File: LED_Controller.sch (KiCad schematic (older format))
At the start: 35 parts, among them CON1 CONNECTOR, CON2 CONNECTOR, CON3 CONNECTOR, CON4 CONNECTOR, CON5 PWR_CON, CON6 AVR-ISP-10, CON7 AVR-ISP-6, IC1 ATMEGA328P-P, Q1 STS8DN3LLH5, Q2 STS8DN3LLH5, Q3 STS8DN3LLH5

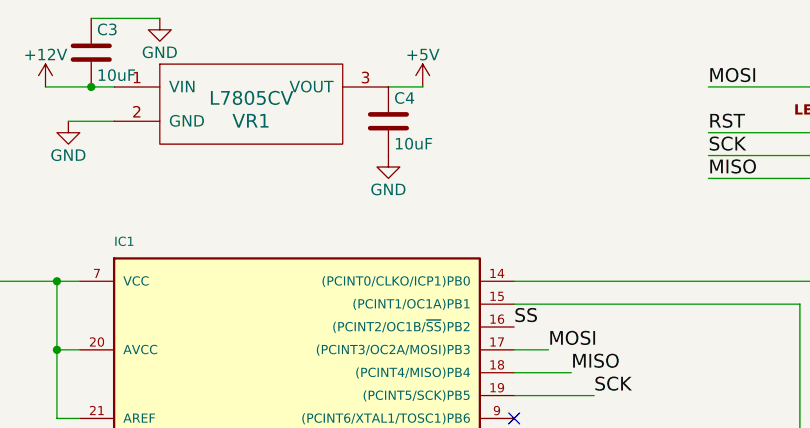
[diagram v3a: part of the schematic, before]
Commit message: Changed passive sizes, re-routed traces
Changed all passive components to 1206 size (that size is stocked in
the lab, and it should be easier to solder without a scope)

Created a general 1206 footprint for resistors and capacitors

Re-routed traces to MOSFETs and rotary encoders, tried to minimize
number of vias
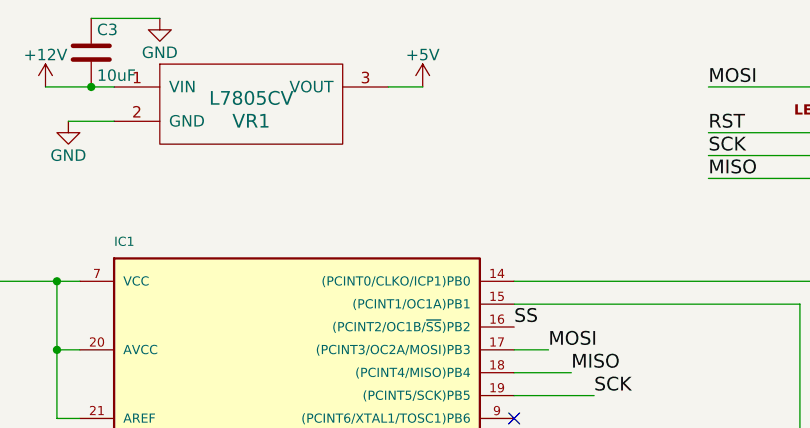
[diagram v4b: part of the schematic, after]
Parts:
- removed C4: 10uF, Capacitors_SMD:C_0603_HandSoldering, symbol C
- C1, C2, R3, R4, R5: footprint Capacitors_SMD:C_0603_HandSoldering -> LED_controller_footprints:SMD_1206
- C3: footprint SMD_Packages:SMD-1206_Pol -> LED_controller_footprints:SMD_1206
- R1, R10, R11, R12, R2, R6, R7: footprint LEDs:LED_0603 -> LED_controller_footprints:SMD_1206
- R8, R9: footprint LEDs:LED_1206 -> LED_controller_footprints:SMD_1206
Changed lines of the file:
@@
 F 0 "R1" V 2130 5350 50  0000 C CNN
 F 1 "10k" V 2050 5350 50  0000 C CNN
-F 2 "LEDs:LED_0603" V 1980 5350 30  0001 C CNN
+F 2 "LED_controller_footprints:SMD_1206" V 1980 5350 30  0001 C CNN
 F 3 "" H 2050 5350 30  0000 C CNN
 	1    2050 5350
@@
 F 0 "R2" V 2130 6250 50  0000 C CNN
 F 1 "10k" V 2050 6250 50  0000 C CNN
-F 2 "LEDs:LED_0603" V 1980 6250 30  0001 C CNN
+F 2 "LED_controller_footprints:SMD_1206" V 1980 6250 30  0001 C CNN
 F 3 "" H 2050 6250 30  0000 C CNN
 	1    2050 6250
@@
 F 0 "R3" V 2130 7250 50  0000 C CNN
 F 1 "10k" V 2050 7250 50  0000 C CNN
-F 2 "Capacitors_SMD:C_0603_HandSoldering" V 1980 7250 30  0001 C CNN
+F 2 "LED_controller_footprints:SMD_1206" V 1980 7250 30  0001 C CNN
 F 3 "" H 2050 7250 30  0000 C CNN
 	1    2050 7250
@@
 F 0 "C1" H 775 2450 50  0000 L CNN
 F 1 "10uF" H 775 2250 50  0000 L CNN
-F 2 "Capacitors_SMD:C_0603_HandSoldering" H 788 2200 30  0001 C CNN
+F 2 "LED_controller_footprints:SMD_1206" H 788 2200 30  0001 C CNN
 F 3 "" H 750 2350 60  0000 C CNN
 	1    750  2350
@@
 F 0 "C2" H 1075 2450 50  0000 L CNN
 F 1 ".1uF" H 1075 2250 50  0000 L CNN
-F 2 "Capacitors_SMD:C_0603_HandSoldering" H 1088 2200 30  0001 C CNN
+F 2 "LED_controller_footprints:SMD_1206" H 1088 2200 30  0001 C CNN
 F 3 "" H 1050 2350 60  0000 C CNN
 	1    1050 2350
@@
 F 0 "R4" V 3830 5000 50  0000 C CNN
 F 1 "10k" V 3750 5000 50  0000 C CNN
-F 2 "Capacitors_SMD:C_0603_HandSoldering" V 3680 5000 30  0001 C CNN
+F 2 "LED_controller_footprints:SMD_1206" V 3680 5000 30  0001 C CNN
 F 3 "" H 3750 5000 30  0000 C CNN
 	1    3750 5000
@@
 F 0 "R5" V 3830 5900 50  0000 C CNN
 F 1 "10k" V 3750 5900 50  0000 C CNN
-F 2 "Capacitors_SMD:C_0603_HandSoldering" V 3680 5900 30  0001 C CNN
+F 2 "LED_controller_footprints:SMD_1206" V 3680 5900 30  0001 C CNN
 F 3 "" H 3750 5900 30  0000 C CNN
 	1    3750 5900
@@
 F 0 "R6" V 3830 6900 50  0000 C CNN
 F 1 "10k" V 3750 6900 50  0000 C CNN
-F 2 "LEDs:LED_0603" V 3680 6900 30  0001 C CNN
+F 2 "LED_controller_footprints:SMD_1206" V 3680 6900 30  0001 C CNN
 F 3 "" H 3750 6900 30  0000 C CNN
 	1    3750 6900
@@
 F 0 "C3" H 2125 950 50  0000 L CNN
 F 1 "10uF" H 2125 750 50  0000 L CNN
-F 2 "SMD_Packages:SMD-1206_Pol" H 2138 700 30  0001 C CNN
+F 2 "LED_controller_footprints:SMD_1206" H 2138 700 30  0001 C CNN
 F 3 "" H 2100 850 60  0000 C CNN
 	1    2100 850
-	1    0    0    -1
-$EndComp
-$Comp
-L C C4
-U 1 1 56B785EB
-P 3400 1150
-F 0 "C4" H 3425 1250 50  0000 L CNN
-F 1 "10uF" H 3425 1050 50  0000 L CNN
-F 2 "Capacitors_SMD:C_0603_HandSoldering" H 3438 1000 30  0001 C CNN
-F 3 "" H 3400 1150 60  0000 C CNN
-	1    3400 1150
-	1    0    0    -1
-$EndComp
-$Comp
-L GND #PWR015
-U 1 1 56B786A8
-P 3400 1300
-F 0 "#PWR015" H 3400 1050 50  0001 C CNN
-F 1 "GND" H 3400 1150 50  0000 C CNN
-F 2 "" H 3400 1300 60  0000 C CNN
-F 3 "" H 3400 1300 60  0000 C CNN
-	1    3400 1300
 	1    0    0    -1
 $EndComp
@@
 F 0 "R7" V 1580 3150 50  0000 C CNN
 F 1 "10k" V 1500 3150 50  0000 C CNN
-F 2 "LEDs:LED_0603" V 1430 3150 30  0001 C CNN
+F 2 "LED_controller_footprints:SMD_1206" V 1430 3150 30  0001 C CNN
 F 3 "" H 1500 3150 30  0000 C CNN
 	1    1500 3150
@@
 F 0 "R8" V 780 5600 50  0000 C CNN
 F 1 "820" V 700 5600 50  0000 C CNN
-F 2 "LEDs:LED_1206" V 630 5600 30  0001 C CNN
+F 2 "LED_controller_footprints:SMD_1206" V 630 5600 30  0001 C CNN
 F 3 "" H 700 5600 30  0000 C CNN
 	1    700  5600
@@
 F 0 "R9" V 1130 5600 50  0000 C CNN
 F 1 "499" V 1050 5600 50  0000 C CNN
-F 2 "LEDs:LED_1206" V 980 5600 30  0001 C CNN
+F 2 "LED_controller_footprints:SMD_1206" V 980 5600 30  0001 C CNN
 F 3 "" H 1050 5600 30  0000 C CNN
 	1    1050 5600
@@
 F 0 "R10" V 5980 2600 50  0000 C CNN
 F 1 "10k" V 5900 2600 50  0000 C CNN
-F 2 "LEDs:LED_0603" V 5830 2600 30  0001 C CNN
+F 2 "LED_controller_footprints:SMD_1206" V 5830 2600 30  0001 C CNN
 F 3 "" H 5900 2600 30  0000 C CNN
 	1    5900 2600
@@
 F 0 "R11" V 5980 3700 50  0000 C CNN
 F 1 "10k" V 5900 3700 50  0000 C CNN
-F 2 "LEDs:LED_0603" V 5830 3700 30  0001 C CNN
+F 2 "LED_controller_footprints:SMD_1206" V 5830 3700 30  0001 C CNN
 F 3 "" H 5900 3700 30  0000 C CNN
 	1    5900 3700
@@
 F 0 "R12" V 5980 4950 50  0000 C CNN
 F 1 "10k" V 5900 4950 50  0000 C CNN
-F 2 "LEDs:LED_0603" V 5830 4950 30  0001 C CNN
+F 2 "LED_controller_footprints:SMD_1206" V 5830 4950 30  0001 C CNN
 F 3 "" H 5900 4950 30  0000 C CNN
 	1    5900 4950

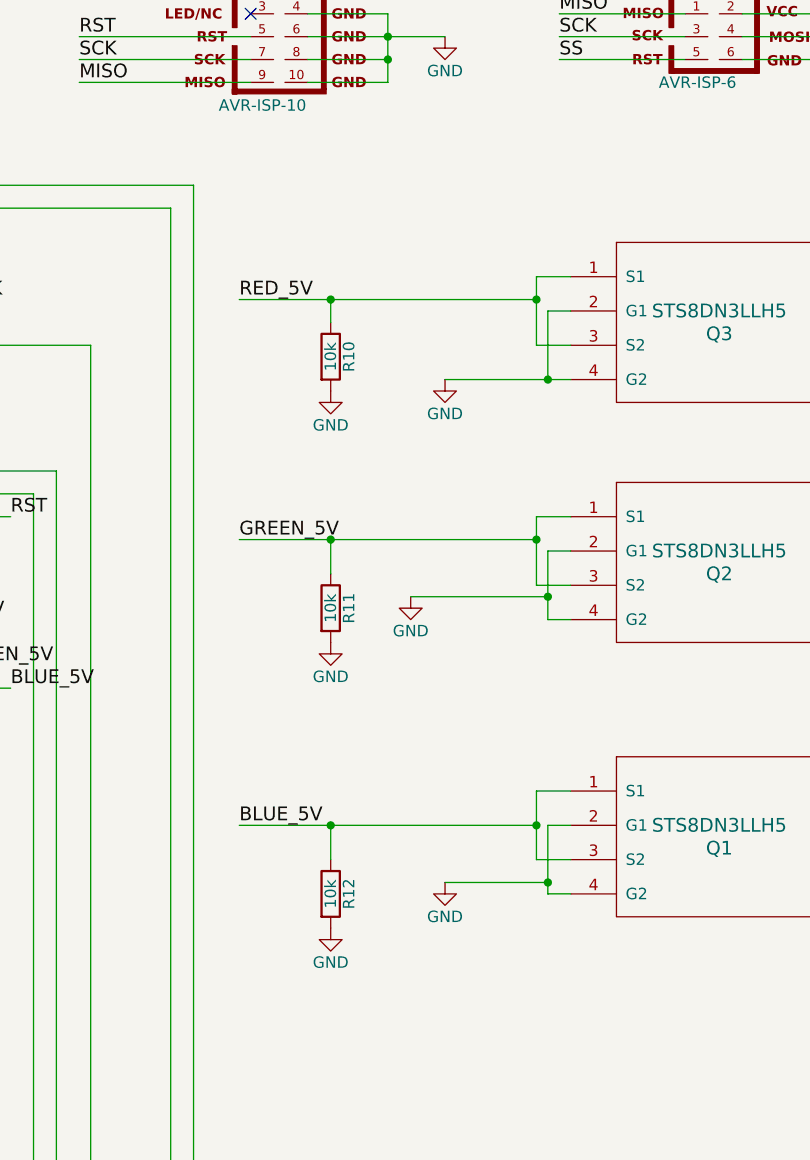
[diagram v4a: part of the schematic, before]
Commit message: Rewired FETs
corrected incorrectly wired MOSFETs in schematic, updated traces
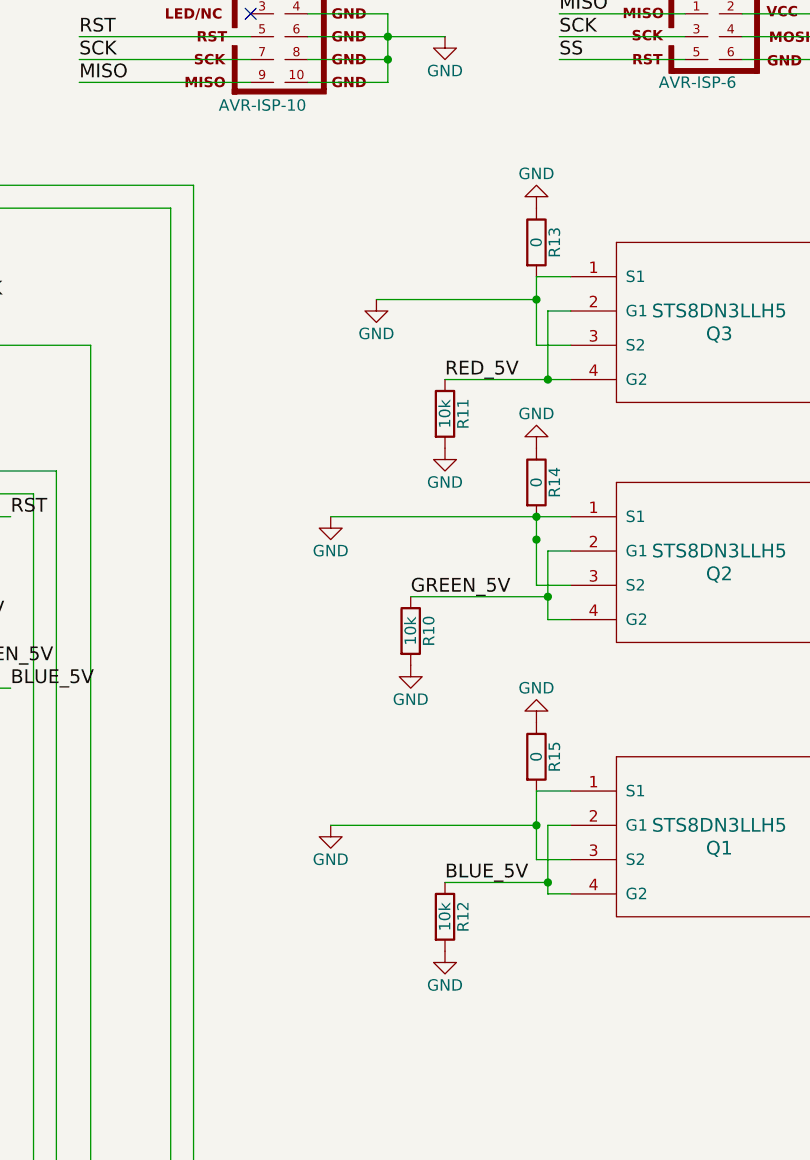
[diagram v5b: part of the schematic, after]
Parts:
- added R13, R14, R15: 0, LED_controller_footprints:SMD_1206, symbol R
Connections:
- net BLUE_5V: now also Q1.2 (G1), Q1.4 (G2); no longer Q1.1 (S1), Q1.3 (S2)
- net GND: now also Q1.1 (S1), Q1.3 (S2), Q2.1 (S1), Q2.3 (S2), Q3.1 (S1), Q3.3 (S2), R13.1, R13.2, R14.1, R14.2, R15.1, R15.2; no longer Q1.2 (G1), Q1.4 (G2), Q2.2 (G1), Q2.4 (G2), Q3.2 (G1), Q3.4 (G2)
- net GREEN_5V: now also Q2.2 (G1), Q2.4 (G2), R10.1; no longer Q2.1 (S1), Q2.3 (S2), R11.1
- net RED_5V: now also Q3.2 (G1), Q3.4 (G2), R11.1; no longer Q3.1 (S1), Q3.3 (S2), R10.1
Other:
- moved on the sheet: R12

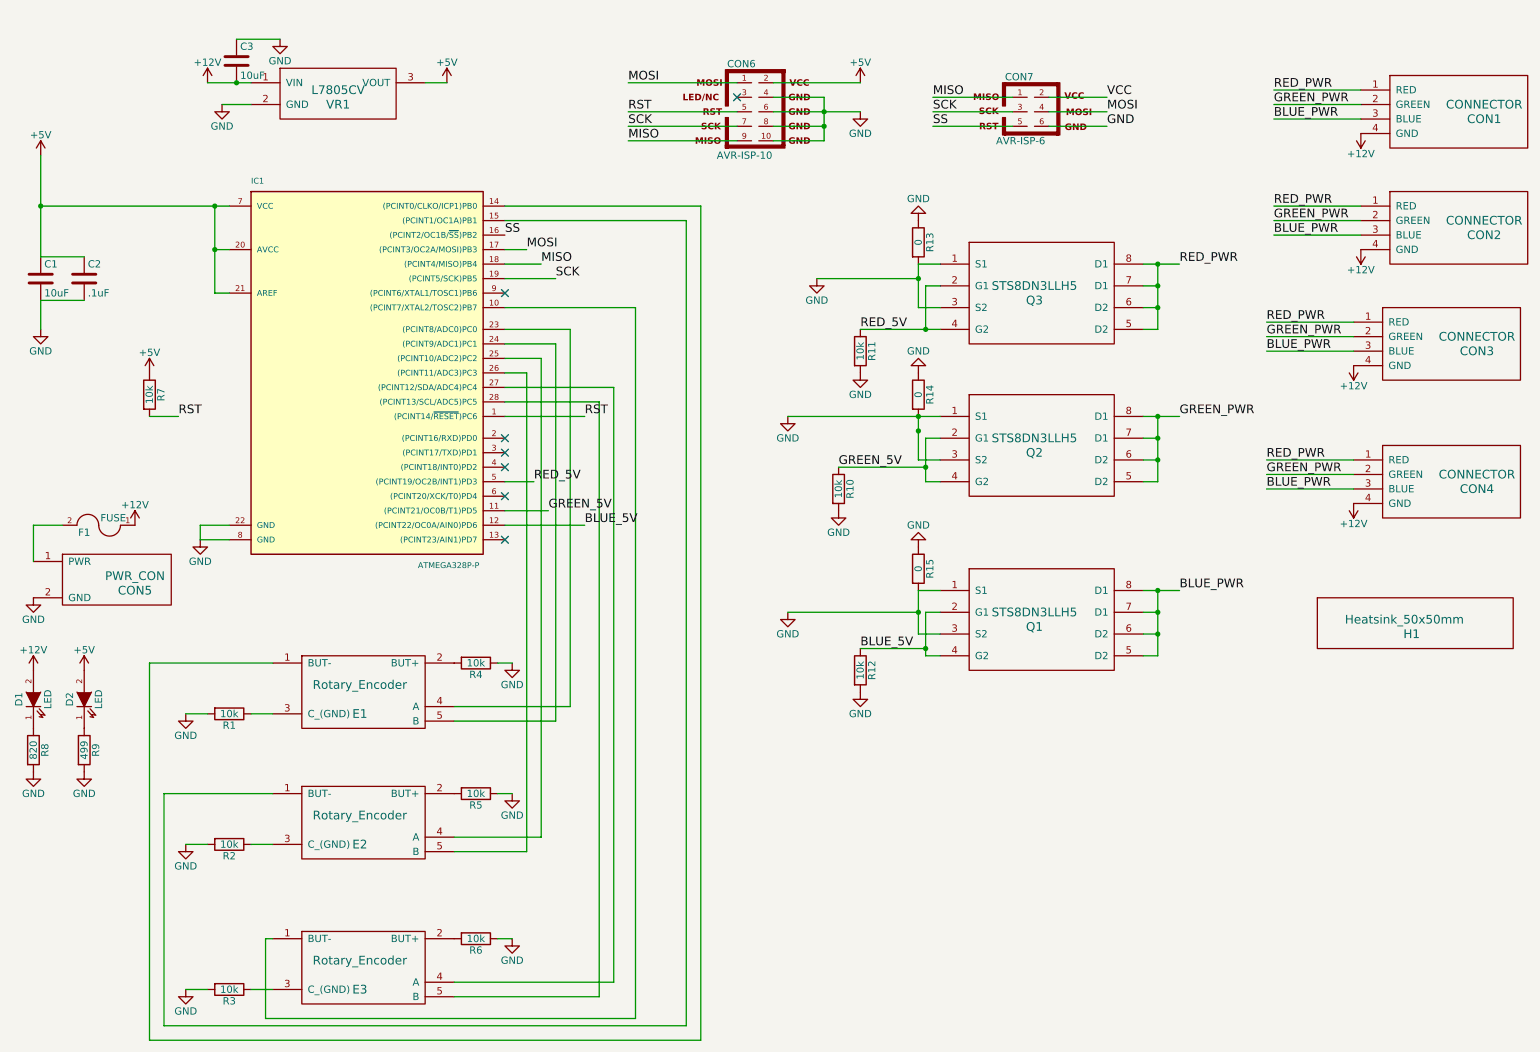
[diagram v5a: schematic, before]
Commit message: Changed some encoder pins, wired outputs for I2C instead os SPI, generated gerber for milling
Re-adjusted resistors to ensure proper milling

Removed 6-pin header for SPI

Added schematic and component for 2-terminal screw block

Wired SCL and SDA to terminal block, added another terminal block for
GND and +5V and routed traces

Re-wired and traced pins for rotary encoder 3 to PD0 and PD1 (they were
connected to SCL and SDA before)

Generated Gerber files for milling
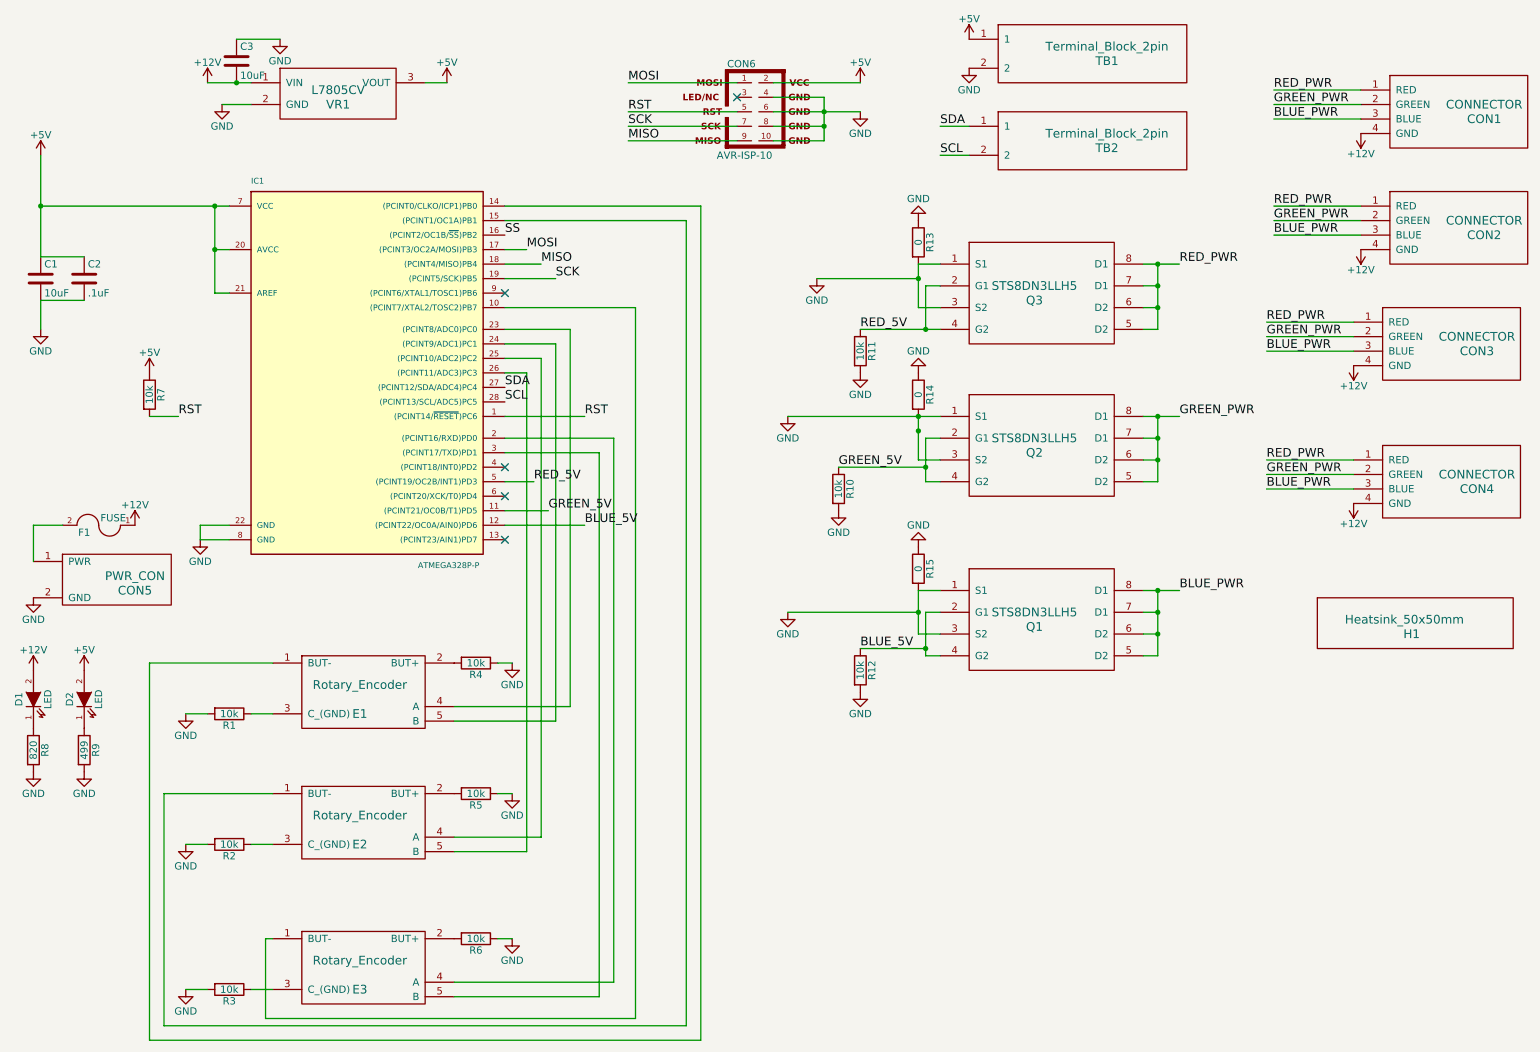
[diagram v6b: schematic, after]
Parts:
- removed CON7: AVR-ISP-6, Connect:PINHEAD1-6, symbol AVR-ISP-6
- added TB1, TB2: Terminal_Block_2pin, LED_controller_footprints:Screw_Terminal, symbol Terminal_Block_2pin
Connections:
- net +5V: now also TB1.1
- net GND: now also TB1.2
- net at IC1.2 ((PCINT16/RXD)PD0): now also E3.4 (A)
- net SDA: now reaches IC1.27 ((PCINT12/SDA/ADC4)PC4)
- net SDA: now also TB2.1; no longer E3.4 (A)
- net at E3.5 (B): now also IC1.3 ((PCINT17/TXD)PD1); no longer IC1.28 ((PCINT13/SCL/ADC5)PC5)
- new net SCL: IC1.28 ((PCINT13/SCL/ADC5)PC5), TB2.2
- no-connect marks 7 -> 5
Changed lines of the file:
@@
 $EndComp
 NoConn ~ 3950 2450
-NoConn ~ 3950 3450
-NoConn ~ 3950 3550
 NoConn ~ 3950 3650
 NoConn ~ 3950 3850
@@
 	1    0    0    -1
 $EndComp
-$Comp
-L AVR-ISP-6 CON7
-U 1 1 56B93EA8
-P 7600 1200
-F 0 "CON7" H 7495 1440 50  0000 C CNN
-F 1 "AVR-ISP-6" H 7335 970 50  0000 L BNN
-F 2 "Connect:PINHEAD1-6" V 7080 1240 50  0001 C CNN
-F 3 "" H 7575 1200 60  0000 C CNN
-	1    7600 1200
-	1    0    0    -1
-$EndComp
 Connection ~ 6800 3400
 Wire Wire Line
@@
 	6950 2250 6800 2250
 Wire Wire Line
-	4600 3200 3950 3200
-Wire Wire Line
-	4600 7300 4600 3200
+	4600 7300 4600 3550
 Wire Wire Line
 	3600 7300 4600 7300
 Wire Wire Line
-	4700 3100 3950 3100
-Wire Wire Line
-	4700 7200 4700 3100
+	4700 7200 4700 3450
 Wire Wire Line
 	3600 7200 4700 7200
@@
 Wire Wire Line
 	9850 2050 9250 2050
-Wire Wire Line
-	6900 1100 7450 1100
-Wire Wire Line
-	7450 1200 6900 1200
-Wire Wire Line
-	7450 1300 6900 1300
-Wire Wire Line
-	7700 1100 8100 1100
-Wire Wire Line
-	7700 1200 8100 1200
-Wire Wire Line
-	7700 1300 8100 1300
-Text Label 6900 1100 0    60   ~ 0
-MISO
-Text Label 6900 1200 0    60   ~ 0
-SCK
-Text Label 8100 1100 0    60   ~ 0
-VCC
-Text Label 8100 1200 0    60   ~ 0
-MOSI
-Text Label 8100 1300 0    60   ~ 0
-GND
 Wire Wire Line
 	2400 700  2100 700
@@
 Text Label 3950 2050 0    60   ~ 0
 SS
-Text Label 6900 1300 0    60   ~ 0
-SS
 $Comp
 L Heatsink_50x50mm H1
@@
 	-1   0    0    1
 $EndComp
+Wire Wire Line
+	4700 3450 3950 3450
+Wire Wire Line
+	4600 3550 3950 3550
+Text Label 3950 3100 0    60   ~ 0
+SDA
+Text Label 3950 3200 0    60   ~ 0
+SCL
+$Comp
+L Terminal_Block_2pin TB1
+U 1 1 56CA882A
+P 8100 850
+F 0 "TB1" H 8100 850 60  0000 C CNN
+F 1 "Terminal_Block_2pin" H 8100 950 60  0000 C CNN
+F 2 "LED_controller_footprints:Screw_Terminal" H 8100 850 60  0001 C CNN
+F 3 "" H 8100 850 60  0000 C CNN
+	1    8100 850
+	1    0    0    -1
+$EndComp
+$Comp
+L GND #PWR036
+U 1 1 56CA88BD
+P 7150 900
+F 0 "#PWR036" H 7150 650 50  0001 C CNN
+F 1 "GND" H 7150 750 50  0000 C CNN
+F 2 "" H 7150 900 60  0000 C CNN
+F 3 "" H 7150 900 60  0000 C CNN
+	1    7150 900
+	1    0    0    -1
+$EndComp
+$Comp
+L +5V #PWR037
+U 1 1 56CA8940
+P 7150 700
+F 0 "#PWR037" H 7150 550 50  0001 C CNN
+F 1 "+5V" H 7150 840 50  0000 C CNN
+F 2 "" H 7150 700 60  0000 C CNN
+F 3 "" H 7150 700 60  0000 C CNN
+	1    7150 700
+	1    0    0    -1
+$EndComp
+$Comp
+L Terminal_Block_2pin TB2
+U 1 1 56CA89F0
+P 8100 1450
+F 0 "TB2" H 8100 1450 60  0000 C CNN
+F 1 "Terminal_Block_2pin" H 8100 1550 60  0000 C CNN
+F 2 "LED_controller_footprints:Screw_Terminal" H 8100 1450 60  0001 C CNN
+F 3 "" H 8100 1450 60  0000 C CNN
+	1    8100 1450
+	1    0    0    -1
+$EndComp
+Text Label 6950 1300 0    60   ~ 0
+SDA
+Text Label 6950 1500 0    60   ~ 0
+SCL
+Wire Wire Line
+	7150 1300 6950 1300
+Wire Wire Line
+	7150 1500 6950 1500
 $EndSCHEMATC
